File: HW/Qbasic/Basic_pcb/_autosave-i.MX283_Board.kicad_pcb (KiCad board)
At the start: 4 copper layers, 73 x 73 mm, 151 parts, among them P1 CONN_02X02, U11 ZLDO1117G33TA, X401 12MHz

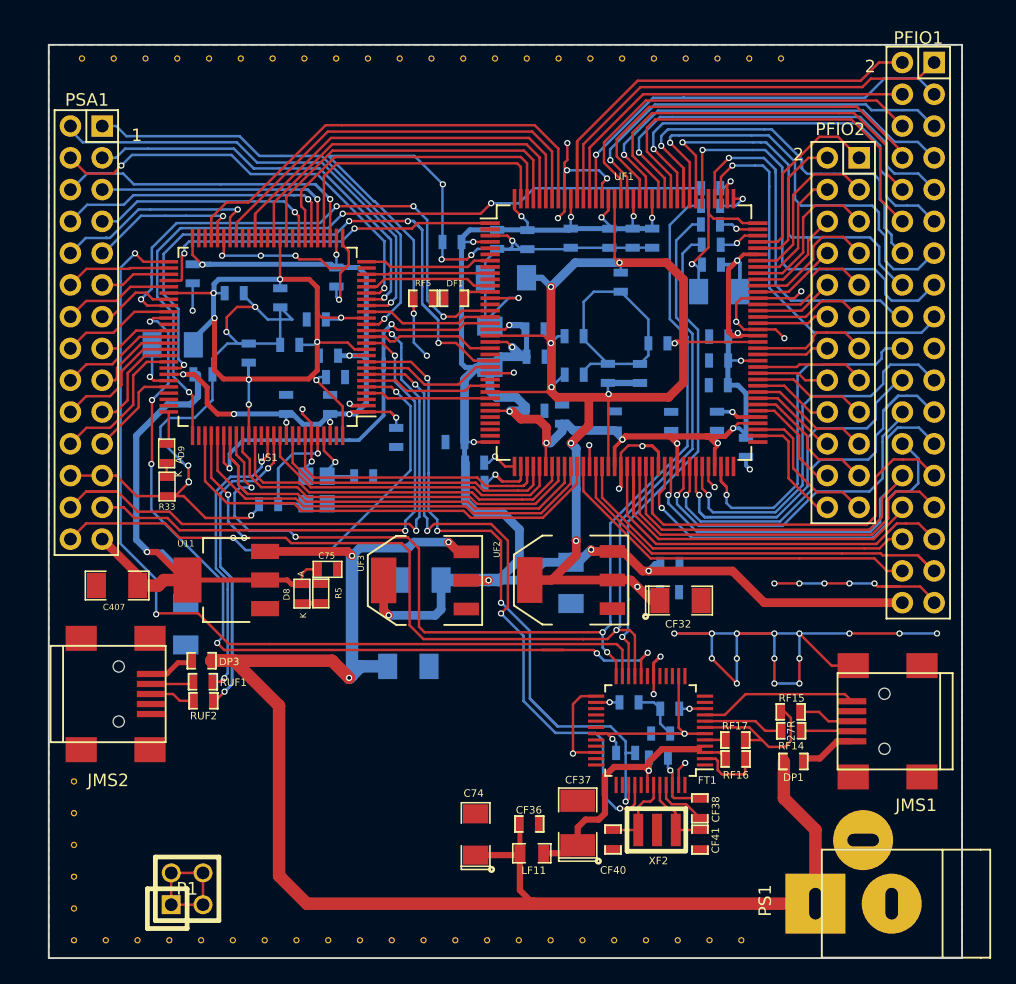
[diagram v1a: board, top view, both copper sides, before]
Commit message: last changes
all components placed, routes traced, ground shields missing
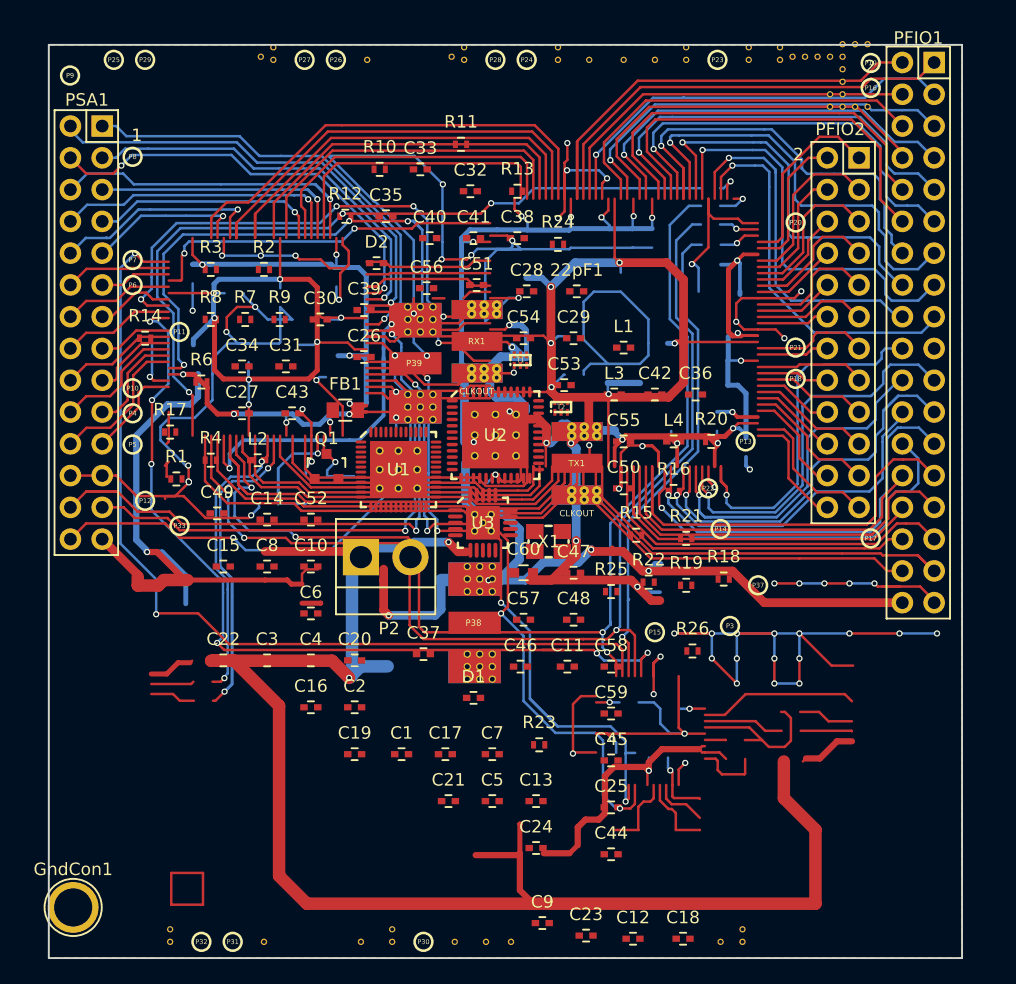
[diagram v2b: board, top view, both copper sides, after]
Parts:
- removed C396, C397, C398, C399, C400, C401, C404, C405, C408, C409, C410, CF1, CF10, CF11, CF12, CF13, CF16, CF17, CF18, CF19, CF2, CF20, CF23, CF24, CF25, CF26, CF27, CF3, CF4, CF5, CF6, CF7, CF8, CF9: 0.1uF, SM0603
- removed C402, C403: 20pF, SM0603
- removed C406, C411, CF14, CF21, CF28: 1uF, SM0603
- removed C407, C412: 4.7uF, SM1206
- removed C74, C76: 33uF, SM1206
- removed C75, CF31, CF33: 100n, SM0603
- removed CF15, CF22, CF29: 4.7uF, SM1206_Opendous
- removed CF30, CF32, CF34, CF35: 33uF, SM1206_Opendous
- removed CF36: 10nF, opendous:SM0603_Opendous
- removed CF37: 10uF, opendous:SM1210_Opendous
- removed CF38: 100nF, opendous:SM0603_Opendous
- removed CF39: 33nF, opendous:SM0603_Opendous
- removed CF40, CF41: 47pF, opendous:SM0603_Opendous
- removed D8, D9, DF1: LED, SM0603
- removed DP1, DP3: DIODE, opendous:SM0603_Opendous
- removed FT1: FT2232D, Housings_QFP:LQFP-48_7x7mm_Pitch0.5mm
- removed JMS1, JMS2: USB-MINI, Connect:USB_Mini-B
- removed LF11: HZ0805D152R-10, opendous:SM0805
- removed P1: CONN_02X02, hackrf:GSG-HEADER-2x2
- removed PS1: BARREL_JACK, Connect:JACK_ALIM
- removed R33, R5, RF5: 1k, SM0603
- removed RF1: 47k, SM0603
- removed RF14, RF15: 27R, opendous:SM0603_Opendous
- removed RF16: 10K, opendous:SM0603_Opendous
- removed RF17: 1K5, opendous:SM0603_Opendous
- removed RF18: 470R, opendous:SM0603_Opendous
- removed RF19, RF20: 10k, opendous:SM0603_Opendous
- removed RF2: 4.7k, SM0603
- removed RF21: 15K, opendous:SM0603_Opendous
- removed RF3, RF4, RF6, RF7: 68, SM0603
- removed RUF1, RUF2: 27, SM0603
- removed TH31, TH32, TH36, TH37: CONN_1, opendous:1Pin_12mil_VIA
- removed U11: ZLDO1117G33TA, LT1117
- removed UF1: XC6SLX9-2TQG144C, Housings_QFP:LQFP-144_20x20mm_Pitch0.5mm
- removed UF2: ZLDO1117G12TA, SMD_Packages:SOT-223
- removed UF3: ZLDO1117G33TA, SMD_Packages:SOT-223
- removed US1: ATSAM3S2CA-AU, Housings_QFP:LQFP-100_14x14mm_Pitch0.5mm
- removed X401: 12MHz, ABM8G
- removed XF2: 6MHz, resonator:CSTCR6M00G53Z
- added 22pF1: C_Small, Capacitors_SMD:C_0402, F.Cu at (61.5, 86.0)
- added C1: 22pF, Capacitors_SMD:C_0402, F.Cu at (47.5, 123.0)
- added C10: 22pF, Capacitors_SMD:C_0402, F.Cu at (40.2, 108.0)
- added C11: 10nF, Capacitors_SMD:C_0402, F.Cu at (60.8, 116.0)
- added C12: 100nF, Capacitors_SMD:C_0402, F.Cu at (66.0, 137.8)
- added C13: 2.2uF, Capacitors_SMD:C_0402, F.Cu at (58.2, 126.8)
- added C14: 100nF, Capacitors_SMD:C_0402, F.Cu at (36.8, 104.2)
- added C15: 2.2uF, Capacitors_SMD:C_0402, F.Cu at (33.2, 108.0)
- added C16: 100nF, Capacitors_SMD:C_0402, F.Cu at (40.2, 119.2)
- added C17: 2.2uF, Capacitors_SMD:C_0402, F.Cu at (51.0, 123.0)
- added C18: 100nF, Capacitors_SMD:C_0402, F.Cu at (70.0, 137.8)
- added C19: 2.2uF, Capacitors_SMD:C_0402, F.Cu at (43.8, 123.0)
- added C2: 22pF, Capacitors_SMD:C_0402, F.Cu at (43.8, 119.2)
- added C20: 100nF, Capacitors_SMD:C_0402, F.Cu at (43.8, 115.5)
- added C21: 2.2uF, Capacitors_SMD:C_0402, F.Cu at (51.2, 126.8)
- added C22: 100nF, Capacitors_SMD:C_0402, F.Cu at (33.2, 115.5)
- added C23: 2.2uF, Capacitors_SMD:C_0402, F.Cu at (62.2, 137.5)
- added C24: 100nF, Capacitors_SMD:C_0402, F.Cu at (58.2, 130.5)
- added C25: 100nF, Capacitors_SMD:C_0402, F.Cu at (64.2, 127.2)
- added C26: 22pF, Capacitors_SMD:C_0402, F.Cu at (44.5, 91.2)
- added C27: 22pF, Capacitors_SMD:C_0402, F.Cu at (34.8, 95.8)
- added C28: 330nF, Capacitors_SMD:C_0402, F.Cu at (57.5, 86.0)
- added C29: 330nF, Capacitors_SMD:C_0402, F.Cu at (61.2, 89.8)
- added C3: 22pF, Capacitors_SMD:C_0402, F.Cu at (36.8, 115.5)
- added C30: 10uF, Capacitors_SMD:C_0402, F.Cu at (41.0, 88.2)
- added C31: 22pF, Capacitors_SMD:C_0402, F.Cu at (38.2, 92.0)
- added C32: 330nF, Capacitors_SMD:C_0402, F.Cu at (53.0, 78.0)
- added C33: 22pF, Capacitors_SMD:C_0402, F.Cu at (49.0, 76.2)
- added C34: 22pF, Capacitors_SMD:C_0402, F.Cu at (34.8, 92.0)
- added C35: 22pF, Capacitors_SMD:C_0402, F.Cu at (46.2, 80.0)
- added C36: 3pF, Capacitors_SMD:C_0402, F.Cu at (71.0, 94.2)
- added C37: 1uF, Capacitors_SMD:C_0402, F.Cu at (49.2, 115.0)
- added C38: 22pF, Capacitors_SMD:C_0402, F.Cu at (56.8, 81.8)
- added C39: 22pF, Capacitors_SMD:C_0402, F.Cu at (44.5, 87.5)
- added C4: 10nF, Capacitors_SMD:C_0402, F.Cu at (40.2, 115.5)
- added C40: 22pF, Capacitors_SMD:C_0402, F.Cu at (49.8, 81.8)
- added C41: 22pF, Capacitors_SMD:C_0402, F.Cu at (53.2, 81.8)
- added C42: 3pF, Capacitors_SMD:C_0402, F.Cu at (67.8, 94.2)
- added C43: 180pF, Capacitors_SMD:C_0402, F.Cu at (38.8, 95.8)
- added C44: 100nF, Capacitors_SMD:C_0402, F.Cu at (64.2, 131.0)
- added C45: 100nF, Capacitors_SMD:C_0402, F.Cu at (64.2, 123.5)
- added C46: 2.2uF, Capacitors_SMD:C_0402, F.Cu at (57.0, 116.0)
- added C47: DNP, Capacitors_SMD:C_0402, F.Cu at (61.2, 108.5)
- added C48: DNP, Capacitors_SMD:C_0402, F.Cu at (61.2, 112.2)
- added C49: 33pF, Capacitors_SMD:C_0402, F.Cu at (32.8, 103.8)
- added C5: 10nF, Capacitors_SMD:C_0402, F.Cu at (54.8, 126.8)
- added C50: 3.3nF, Capacitors_SMD:C_0402, F.Cu at (65.2, 101.8)
- added C51: 100pF, Capacitors_SMD:C_0402, F.Cu at (53.5, 85.5)
- added C52: 47pF, Capacitors_SMD:C_0402, F.Cu at (40.2, 104.2)
- added C53: 100pF, Capacitors_SMD:C_0402, F.Cu at (60.5, 93.5)
- added C54: 100pF, Capacitors_SMD:C_0402, F.Cu at (57.2, 89.8)
- added C55: 100pF, Capacitors_SMD:C_0402, F.Cu at (65.2, 98.0)
- added C56: 100pF, Capacitors_SMD:C_0402, F.Cu at (49.5, 85.8)
- added C57: 100nF, Capacitors_SMD:C_0402, F.Cu at (57.2, 112.2)
- added C58: 100nF, Capacitors_SMD:C_0402, F.Cu at (64.2, 116.0)
- added C59: 100nF, Capacitors_SMD:C_0402, F.Cu at (64.2, 119.8)
- added C6: 100pF, Capacitors_SMD:C_0402, F.Cu at (40.2, 111.8)
- added C60: 100nF, Capacitors_SMD:C_0603, F.Cu at (57.2, 108.5)
- added C7: 100nF, Capacitors_SMD:C_0402, F.Cu at (54.8, 123.0)
- added C8: 10nF, Capacitors_SMD:C_0402, F.Cu at (36.8, 108.0)
- added C9: 10nF, Capacitors_SMD:C_0402, F.Cu at (58.8, 136.5)
- added D1: GSG-DIODE-TVS-BI, Capacitors_SMD:C_0402, F.Cu at (53.2, 118.5)
- added D2: GSG-DIODE-TVS-BI, Capacitors_SMD:C_0402, F.Cu at (45.5, 83.8)
- added FB1: FILTER, Capacitors_SMD:C_0805, F.Cu at (43.0, 95.5)
- added GndCon1: GND, Connect:1pin, F.Cu at (21.2, 135.2)
- added L1: DNP, Capacitors_SMD:C_0402, F.Cu at (65.2, 90.5)
- added L2: 6.2nH, Capacitors_SMD:C_0402, F.Cu at (36.0, 99.5)
- added L3: DNP, Capacitors_SMD:C_0402, F.Cu at (64.5, 94.2)
- added L4: DNP, Capacitors_SMD:C_0402, F.Cu at (69.2, 98.0)
- added P10: TXENABLE, hackrf1:GSG-TESTPOINT-50MIL-MASKONLY, F.Cu at (26.0, 93.8)
- added P11: RXENABLE, hackrf1:GSG-TESTPOINT-50MIL-MASKONLY, F.Cu at (29.8, 89.2)
- added P12: XTAL2, hackrf1:GSG-TESTPOINT-50MIL-MASKONLY, F.Cu at (27.0, 102.8)
- added P13: GCK1, hackrf1:GSG-TESTPOINT-50MIL-MASKONLY, F.Cu at (75.0, 98.0)
- added P14: GCK2, hackrf1:GSG-TESTPOINT-50MIL-MASKONLY, F.Cu at (73.0, 105.0)
- added P15: SGPIO_CLK, hackrf1:GSG-TESTPOINT-50MIL-MASKONLY, F.Cu at (67.8, 113.2)
- added P16: DA0, hackrf1:GSG-TESTPOINT-50MIL-MASKONLY, F.Cu at (85.0, 69.8)
- added P17: DA4, hackrf1:GSG-TESTPOINT-50MIL-MASKONLY, F.Cu at (85.0, 105.8)
- added P18: DA7, hackrf1:GSG-TESTPOINT-50MIL-MASKONLY, F.Cu at (79.0, 93.0)
- added P19: DD0, hackrf1:GSG-TESTPOINT-50MIL-MASKONLY, F.Cu at (85.0, 67.8)
- added P2: VAA, Pin_Headers:Pin_Header_Straight_1x02_Pitch3.96mm_Friction_Lock, F.Cu at (44.2, 107.2)
- added P20: DD5, hackrf1:GSG-TESTPOINT-50MIL-MASKONLY, F.Cu at (79.0, 80.5)
- added P21: DD9, hackrf1:GSG-TESTPOINT-50MIL-MASKONLY, F.Cu at (79.0, 90.5)
- added P22: RSSI, hackrf1:GSG-TESTPOINT-50MIL-MASKONLY, F.Cu at (72.0, 101.8)
- added P23: GND, hackrf1:GSG-TESTPOINT-50MIL-MASKONLY, F.Cu at (72.8, 67.5)
- added P24: GND, hackrf1:GSG-TESTPOINT-50MIL-MASKONLY, F.Cu at (57.5, 67.5)
- added P25: GND, hackrf1:GSG-TESTPOINT-50MIL-MASKONLY, F.Cu at (24.5, 67.5)
- added P26: GND, hackrf1:GSG-TESTPOINT-50MIL-MASKONLY, F.Cu at (42.2, 67.5)
- added P27: GND, hackrf1:GSG-TESTPOINT-50MIL-MASKONLY, F.Cu at (39.8, 67.5)
- added P28: GND, hackrf1:GSG-TESTPOINT-50MIL-MASKONLY, F.Cu at (55.0, 67.5)
- added P29: GND, hackrf1:GSG-TESTPOINT-50MIL-MASKONLY, F.Cu at (27.0, 67.5)
- added P3: SCL, hackrf1:GSG-TESTPOINT-50MIL-MASKONLY, F.Cu at (73.8, 112.8)
- added P30: GND, hackrf1:GSG-TESTPOINT-50MIL-MASKONLY, F.Cu at (49.2, 138.0)
- added P31: GND, hackrf1:GSG-TESTPOINT-50MIL-MASKONLY, F.Cu at (34.0, 138.0)
- added P32: GND, hackrf1:GSG-TESTPOINT-50MIL-MASKONLY, F.Cu at (31.5, 138.0)
- added P33: XCVR_CLKOUT, hackrf1:GSG-TESTPOINT-50MIL-MASKONLY, F.Cu at (29.8, 104.8)
- added P37: INTR, hackrf1:GSG-TESTPOINT-50MIL-MASKONLY, F.Cu at (76.0, 109.5)
- added P38: CLKIN, hackrf1:GSG-SMA-73251-2120, F.Cu at (51.2, 112.5)
- added P39: CLKOUT, hackrf1:GSG-SMA-73251-2120, F.Cu at (46.5, 91.8)
- added P4: SDA, hackrf1:GSG-TESTPOINT-50MIL-MASKONLY, F.Cu at (26.0, 95.8)
- added P5: SSP1_SCK, hackrf1:GSG-TESTPOINT-50MIL-MASKONLY, F.Cu at (26.0, 98.2)
- added P6: SSP1_MOSI, hackrf1:GSG-TESTPOINT-50MIL-MASKONLY, F.Cu at (26.0, 85.5)
- added P7: SSP1_MISO, hackrf1:GSG-TESTPOINT-50MIL-MASKONLY, F.Cu at (26.0, 83.5)
- added P8: CS_XCVR, hackrf1:GSG-TESTPOINT-50MIL-MASKONLY, F.Cu at (26.0, 75.2)
- added P9: CS_AD, hackrf1:GSG-TESTPOINT-50MIL-MASKONLY, F.Cu at (21.0, 68.8)
- added Q1: MOSFET_P, kicad1:SOT-23mos, F.Cu at (41.5, 100.0)
- added R1: 10k, Resistors_SMD:R_0402, F.Cu at (29.5, 101.0)
- added R10: 0, Resistors_SMD:R_0402, F.Cu at (45.8, 76.2)
- added R11: 0, Resistors_SMD:R_0402, F.Cu at (52.2, 74.2)
- added R12: 0, Resistors_SMD:R_0402, F.Cu at (43.0, 80.0)
- added R13: 0, Resistors_SMD:R_0402, F.Cu at (56.8, 78.0)
- added R14: 10k, Resistors_SMD:R_0402, F.Cu at (27.0, 89.8)
- added R15: 475, Resistors_SMD:R_0402, F.Cu at (66.2, 105.5)
- added R16: 475, Resistors_SMD:R_0402, F.Cu at (69.2, 102.0)
- added R17: 1k8, Resistors_SMD:R_0402, F.Cu at (29.0, 97.2)
- added R18: 1k8, Resistors_SMD:R_0402, F.Cu at (73.2, 109.0)
- added R19: 10k, Resistors_SMD:R_0402, F.Cu at (70.2, 109.5)
- added R2: 1k, Resistors_SMD:R_0402, F.Cu at (36.5, 84.2)
- added R20: 39, Resistors_SMD:R_0402, F.Cu at (72.2, 98.0)
- added R21: 39, Resistors_SMD:R_0402, F.Cu at (70.2, 105.8)
- added R22: 39, Resistors_SMD:R_0402, F.Cu at (67.2, 109.2)
- added R23: 10k, Resistors_SMD:R_0402, F.Cu at (58.5, 122.2)
- added R24: 39, Resistors_SMD:R_0402, F.Cu at (60.0, 82.2)
- added R25: 10k, Resistors_SMD:R_0402, F.Cu at (64.2, 110.0)
- added R26: 0, Resistors_SMD:R_0402, F.Cu at (70.8, 114.8)
- added R3: 1k, Resistors_SMD:R_0402, F.Cu at (32.2, 84.2)
- added R4: 1k, Resistors_SMD:R_0402, F.Cu at (32.2, 99.5)
- added R6: 4k7, Resistors_SMD:R_0402, F.Cu at (31.5, 93.2)
- added R7: 4k7, Resistors_SMD:R_0402, F.Cu at (35.0, 88.2)
- added R8: 4k7, Resistors_SMD:R_0402, F.Cu at (32.2, 88.2)
- added R9: 4k7, Resistors_SMD:R_0402, F.Cu at (37.8, 88.2)
- added RX1: CLKOUT, hackrf1:GSG-SMA-EDGE, F.Cu at (51.5, 90.0)
- added T1: RX_BALUN, hackrf1:GSG-2500BL14M100, F.Cu at (57.0, 91.5)
- added T2: TX_BALUN, hackrf1:GSG-2500BL14M100, F.Cu at (60.2, 95.2)
- added TX1: CLKOUT, hackrf1:GSG-SMA-EDGE, F.Cu at (59.5, 99.8)
- added U1: MAX2837, hackrf1:GSG-QFN48-6, F.Cu at (47.2, 100.2)
- added U2: MAX5864, hackrf1:GSG-QFN48-7, F.Cu at (55.0, 97.5)
- added U3: SI5351C, hackrf1:GSG-QFN20-4, F.Cu at (54.0, 104.5)
- added X1: GSG-XTAL4PIN, hackrf1:GSG-XTAL3.2x2.5mm, F.Cu at (59.2, 106.0)
- PFIO2: value CONN_02X13 -> CONN_02X12
- moved TH35 93.1 mm to (83.8, 66.2)
- moved TH12 88.0 mm to (75.2, 66.5)
- moved TH7 83.7 mm to (77.8, 66.5)
- moved TH10 76.9 mm to (62.5, 67.5)
- moved TH8 76.4 mm to (37.2, 66.5)
- moved TH20 75.9 mm to (77.8, 67.5)
- moved TH4 75.2 mm to (82.8, 67.2)
- moved TH5 75.2 mm to (36.2, 67.2)
- moved TH2 75.2 mm to (70.2, 66.5)
- moved TH6 74.1 mm to (51.5, 67.2)
- moved TH24 74.0 mm to (51.8, 138.0)
- moved TH16 73.2 mm to (78.8, 67.2)
- moved TH9 71.9 mm to (80.8, 67.2)
- moved TH43 71.8 mm to (73.0, 138.0)
- moved TH11 71.4 mm to (79.8, 67.2)
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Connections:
- PFIO1 pad 1: /spartan6/IO72 -> DA0
- PFIO1 pad 10: /spartan6/IO65 -> DD4
- PFIO1 pad 11: /spartan6/IO62 -> Net-(PFIO1-Pad11)
- PFIO1 pad 12: /spartan6/IO63 -> DD5
- PFIO1 pad 13: /spartan6/IO60 -> Net-(PFIO1-Pad13)
- PFIO1 pad 14: /spartan6/IO61 -> DD6
- PFIO1 pad 15: /spartan6/IO58 -> Net-(PFIO1-Pad15)
- PFIO1 pad 16: /spartan6/IO59 -> DD7
- PFIO1 pad 17: /spartan6/IO56 -> Net-(PFIO1-Pad17)
- PFIO1 pad 18: /spartan6/IO57 -> DD8
- PFIO1 pad 19: GND -> Net-(PFIO1-Pad19)
- PFIO1 pad 2: /spartan6/IO73 -> DD0
- PFIO1 pad 20: /spartan6/IO31 -> DD9
- PFIO1 pad 21: /spartan6/IO30 -> Net-(PFIO1-Pad21)
- PFIO1 pad 22: /spartan6/IO29 -> DA7
- PFIO1 pad 23: /spartan6/IO28 -> Net-(PFIO1-Pad23)
- PFIO1 pad 24: /spartan6/IO27 -> DA6
- PFIO1 pad 25: /spartan6/IO26 -> Net-(PFIO1-Pad25)
- PFIO1 pad 26: /spartan6/IO25 -> DA5
- PFIO1 pad 27: /spartan6/IO24 -> Net-(PFIO1-Pad27)
- PFIO1 pad 28: /spartan6/IO23 -> DA4
- PFIO1 pad 29: /spartan6/IO22 -> Net-(PFIO1-Pad29)
- PFIO1 pad 3: /spartan6/IO70 -> Net-(PFIO1-Pad3)
- PFIO1 pad 30: /spartan6/IO21 -> DA3
- PFIO1 pad 31: /spartan6/IO20 -> Net-(PFIO1-Pad31)
- PFIO1 pad 32: /spartan6/IO19 -> DA2
- PFIO1 pad 33: /spartan6/IO18 -> Net-(PFIO1-Pad33)
- PFIO1 pad 34: /spartan6/IO17 -> DA1
- PFIO1 pad 35: GND -> Net-(PFIO1-Pad35)
- PFIO1 pad 36: +3.3VDAC -> VCC
- PFIO1 pad 4: /spartan6/IO71 -> DD1
- PFIO1 pad 5: /spartan6/IO68 -> Net-(PFIO1-Pad5)
- PFIO1 pad 6: /spartan6/IO69 -> DD2
- PFIO1 pad 7: /spartan6/IO66 -> Net-(PFIO1-Pad7)
- PFIO1 pad 8: /spartan6/IO67 -> DD3
- PFIO1 pad 9: /spartan6/IO64 -> Net-(PFIO1-Pad9)
- PFIO2 pad 1: /spartan6/IO55 -> Net-(PFIO2-Pad1)
- PFIO2 pad 10: /spartan6/IO46 -> Net-(PFIO2-Pad10)
- PFIO2 pad 11: /spartan6/IO45 -> Net-(PFIO2-Pad11)
- PFIO2 pad 12: /spartan6/IO44 -> Net-(PFIO2-Pad12)
- PFIO2 pad 13: /spartan6/IO43 -> Net-(PFIO2-Pad13)
- PFIO2 pad 14: /spartan6/IO42 -> Net-(PFIO2-Pad14)
- PFIO2 pad 15: /spartan6/IO41 -> Net-(PFIO2-Pad15)
- PFIO2 pad 16: /spartan6/IO40 -> Net-(PFIO2-Pad16)
- PFIO2 pad 17: /spartan6/IO39 -> Net-(PFIO2-Pad17)
- PFIO2 pad 18: /spartan6/IO38 -> Net-(PFIO2-Pad18)
- PFIO2 pad 19: /spartan6/IO37 -> Net-(PFIO2-Pad19)
- PFIO2 pad 2: /spartan6/IO54 -> Net-(PFIO2-Pad2)
- PFIO2 pad 20: /spartan6/IO36 -> Net-(PFIO2-Pad20)
- PFIO2 pad 21: /spartan6/IO35 -> Net-(PFIO2-Pad21)
- PFIO2 pad 22: /spartan6/IO34 -> Net-(PFIO2-Pad22)
- PFIO2 pad 23: /spartan6/IO33 -> Net-(PFIO2-Pad23)
- PFIO2 pad 24: /spartan6/IO32 -> Net-(PFIO2-Pad24)
- PFIO2 pad 3: /spartan6/IO53 -> Net-(PFIO2-Pad3)
- PFIO2 pad 4: /spartan6/IO52 -> Net-(PFIO2-Pad4)
- PFIO2 pad 5: /spartan6/IO51 -> Net-(PFIO2-Pad5)
- PFIO2 pad 6: /spartan6/IO50 -> Net-(PFIO2-Pad6)
- PFIO2 pad 7: /spartan6/IO49 -> Net-(PFIO2-Pad7)
- PFIO2 pad 8: /spartan6/IO48 -> Net-(PFIO2-Pad8)
- PFIO2 pad 9: /spartan6/IO47 -> Net-(PFIO2-Pad9)
- PSA1 pad 1: /SAM3M/AD8 -> !VAA_ENABLE
- PSA1 pad 10: /SAM3M/UTXD0 -> Net-(PSA1-Pad10)
- PSA1 pad 11: /SAM3M/RXD0 -> SSP1_MISO
- PSA1 pad 12: /SAM3M/TXD0 -> SSP1_MOSI
- PSA1 pad 13: /SAM3M/PA27 -> Net-(PSA1-Pad13)
- PSA1 pad 14: /SAM3M/PA4 -> SCL
- PSA1 pad 15: /SAM3M/PC9 -> Net-(PSA1-Pad15)
- PSA1 pad 16: /SAM3M/PA28 -> XCVR_EN
- PSA1 pad 17: /SAM3M/PA30 -> Net-(PSA1-Pad17)
- PSA1 pad 18: /SAM3M/PA29 -> RXENABLE
- PSA1 pad 19: /SAM3M/PA3 -> SDA
- PSA1 pad 2: /SAM3M/AD2 -> CS_AD
- PSA1 pad 20: /SAM3M/PC10 -> TXENABLE
- PSA1 pad 21: /SAM3M/PC14 -> OEB
- PSA1 pad 22: /SAM3M/PA2 -> SSP1_SCK
- PSA1 pad 23: GND -> Net-(PSA1-Pad23)
- PSA1 pad 24: GND -> Net-(PSA1-Pad24)
- PSA1 pad 25: /SAM3M/AD0 -> Net-(PSA1-Pad25)
- PSA1 pad 26: /SAM3M/AD1 -> Net-(PSA1-Pad26)
- PSA1 pad 27: +3.3VP -> Net-(PSA1-Pad27)
- PSA1 pad 28: /SAM3M/AD5 -> Net-(PSA1-Pad28)
- PSA1 pad 3: /SAM3M/AD11 -> Net-(PSA1-Pad3)
- PSA1 pad 4: /SAM3M/AD9 -> CS_XCVR
- PSA1 pad 5: /SAM3M/PWML3 -> Net-(PSA1-Pad5)
- PSA1 pad 6: /SAM3M/PWML2 -> Net-(PSA1-Pad6)
- PSA1 pad 7: /SAM3M/PWMH2 -> Net-(PSA1-Pad7)
- PSA1 pad 8: /SAM3M/PWMH3 -> Net-(PSA1-Pad8)
- PSA1 pad 9: /SAM3M/URXD0 -> Net-(PSA1-Pad9)
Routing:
- net (no net): track 0.00 -> 892.5 mm, vias 0 -> 63
- net GND: track 347.6 -> 941.4 mm, vias 61 -> 56
- net Net-(C30-Pad1): track 0.00 -> 227.3 mm, vias 0 -> 14
- net +3.3VDAC: track 222.4 -> 0.00 mm, vias 22 -> 0
- net VAA: track 0.00 -> 176.0 mm, vias 0 -> 4
- net VDD5V: track 129.1 -> 0.00 mm, vias 3 -> 0
- net +3.3VP: track 121.2 -> 0.00 mm, vias 10 -> 0
- net +1V2: track 119.8 -> 0.00 mm, vias 9 -> 0
- net /spartan6/F_TCK: track 88.4 -> 0.00 mm, vias 4 -> 0
- net /spartan6/F_TMS: track 87.8 -> 0.00 mm, vias 3 -> 0
- net VCC: track 0.00 -> 80.0 mm
- net !VAA_ENABLE: track 0.00 -> 74.5 mm, vias 0 -> 1
- net /SAM3M/JTDI: track 74.3 -> 0.00 mm, vias 2 -> 0
- net /SAM3M/JNRST: track 70.4 -> 0.00 mm, vias 6 -> 0
- net +1.8V: track 67.4 -> 0.00 mm, vias 8 -> 0
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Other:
- board text removed: "A"
- board text removed: "K"

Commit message: version final antes de  planos de tierra
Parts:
- removed 22pF1: C_Small, Capacitors_SMD:C_0402
- removed C1, C10, C2, C26, C27, C3, C31, C33, C34, C35, C38, C39, C40, C41: 22pF, Capacitors_SMD:C_0402
- removed C11, C4, C5, C8, C9: 10nF, Capacitors_SMD:C_0402
- removed C12, C14, C16, C18, C20, C22, C24, C25, C44, C45, C57, C58, C59, C7: 100nF, Capacitors_SMD:C_0402
- removed C13, C15, C17, C19, C21, C23, C46: 2.2uF, Capacitors_SMD:C_0402
- removed C28, C29, C32: 330nF, Capacitors_SMD:C_0402
- removed C30: 10uF, Capacitors_SMD:C_0402
- removed C36, C42: 3pF, Capacitors_SMD:C_0402
- removed C37: 1uF, Capacitors_SMD:C_0402
- removed C43: 180pF, Capacitors_SMD:C_0402
- removed C47, C48, L1, L3, L4: DNP, Capacitors_SMD:C_0402
- removed C49: 33pF, Capacitors_SMD:C_0402
- removed C50: 3.3nF, Capacitors_SMD:C_0402
- removed C51, C53, C54, C55, C56, C6: 100pF, Capacitors_SMD:C_0402
- removed C52: 47pF, Capacitors_SMD:C_0402
- removed C60: 100nF, Capacitors_SMD:C_0603
- removed D1, D2: GSG-DIODE-TVS-BI, Capacitors_SMD:C_0402
- removed FB1: FILTER, Capacitors_SMD:C_0805
- removed GndCon1: GND, Connect:1pin
- removed L2: 6.2nH, Capacitors_SMD:C_0402
- removed P10: TXENABLE, hackrf1:GSG-TESTPOINT-50MIL-MASKONLY
- removed P11: RXENABLE, hackrf1:GSG-TESTPOINT-50MIL-MASKONLY
- removed P12: XTAL2, hackrf1:GSG-TESTPOINT-50MIL-MASKONLY
- removed P13: GCK1, hackrf1:GSG-TESTPOINT-50MIL-MASKONLY
- removed P14: GCK2, hackrf1:GSG-TESTPOINT-50MIL-MASKONLY
- removed P15: SGPIO_CLK, hackrf1:GSG-TESTPOINT-50MIL-MASKONLY
- removed P16: DA0, hackrf1:GSG-TESTPOINT-50MIL-MASKONLY
- removed P17: DA4, hackrf1:GSG-TESTPOINT-50MIL-MASKONLY
- removed P18: DA7, hackrf1:GSG-TESTPOINT-50MIL-MASKONLY
- removed P19: DD0, hackrf1:GSG-TESTPOINT-50MIL-MASKONLY
- removed P2: VAA, Pin_Headers:Pin_Header_Straight_1x02_Pitch3.96mm_Friction_Lock
- removed P20: DD5, hackrf1:GSG-TESTPOINT-50MIL-MASKONLY
- removed P21: DD9, hackrf1:GSG-TESTPOINT-50MIL-MASKONLY
- removed P22: RSSI, hackrf1:GSG-TESTPOINT-50MIL-MASKONLY
- removed P23, P24, P25, P26, P27, P28, P29, P30, P31, P32: GND, hackrf1:GSG-TESTPOINT-50MIL-MASKONLY
- removed P3: SCL, hackrf1:GSG-TESTPOINT-50MIL-MASKONLY
- removed P33: XCVR_CLKOUT, hackrf1:GSG-TESTPOINT-50MIL-MASKONLY
- removed P37: INTR, hackrf1:GSG-TESTPOINT-50MIL-MASKONLY
- removed P38: CLKIN, hackrf1:GSG-SMA-73251-2120
- removed P39: CLKOUT, hackrf1:GSG-SMA-73251-2120
- removed P4: SDA, hackrf1:GSG-TESTPOINT-50MIL-MASKONLY
- removed P5: SSP1_SCK, hackrf1:GSG-TESTPOINT-50MIL-MASKONLY
- removed P6: SSP1_MOSI, hackrf1:GSG-TESTPOINT-50MIL-MASKONLY
- removed P7: SSP1_MISO, hackrf1:GSG-TESTPOINT-50MIL-MASKONLY
- removed P8: CS_XCVR, hackrf1:GSG-TESTPOINT-50MIL-MASKONLY
- removed P9: CS_AD, hackrf1:GSG-TESTPOINT-50MIL-MASKONLY
- removed Q1: MOSFET_P, kicad1:SOT-23mos
- removed R1, R14, R19, R23, R25: 10k, Resistors_SMD:R_0402
- removed R10, R11, R12, R13, R26: 0, Resistors_SMD:R_0402
- removed R15, R16: 475, Resistors_SMD:R_0402
- removed R17, R18: 1k8, Resistors_SMD:R_0402
- removed R2, R3, R4: 1k, Resistors_SMD:R_0402
- removed R20, R21, R22, R24: 39, Resistors_SMD:R_0402
- removed R6, R7, R8, R9: 4k7, Resistors_SMD:R_0402
- removed RX1, TX1: CLKOUT, hackrf1:GSG-SMA-EDGE
- removed T1: RX_BALUN, hackrf1:GSG-2500BL14M100
- removed T2: TX_BALUN, hackrf1:GSG-2500BL14M100
- removed U1: MAX2837, hackrf1:GSG-QFN48-6
- removed U2: MAX5864, hackrf1:GSG-QFN48-7
- removed U3: SI5351C, hackrf1:GSG-QFN20-4
- removed X1: GSG-XTAL4PIN, hackrf1:GSG-XTAL3.2x2.5mm
- added C396: 0.1uF, SM0603, B.Cu at (34.1, 86.2)
- added C397: 0.1uF, SM0603, B.Cu at (38.6, 90.3)
- added C398: 0.1uF, SM0603, B.Cu at (41.8, 95.0)
- added C399: 0.1uF, SM0603, B.Cu at (41.7, 91.2)
- added C400: 0.1uF, SM0603, B.Cu at (38.3, 95.0)
- added C401: 0.1uF, SM0603, B.Cu at (42.3, 84.9)
- added C402: 20pF, SM0603, B.Cu at (44.5, 100.8)
- added C403: 20pF, SM0603, B.Cu at (36.9, 103.0)
- added C404: 0.1uF, SM0603, B.Cu at (30.8, 84.6)
- added C405: 0.1uF, SM0603, B.Cu at (31.6, 92.6)
- added C406: 1uF, SM0603, B.Cu at (47.1, 97.7)
- added C407: 4.7uF, SM1206, F.Cu at (24.8, 109.5)
- added C408: 0.1uF, SM0603, B.Cu at (35.3, 90.9)
- added C409: 0.1uF, SM0603, B.Cu at (42.2, 92.9)
- added C410: 0.1uF, SM0603, B.Cu at (40.7, 88.2)
- added C411: 1uF, SM0603, B.Cu at (37.8, 86.5)
- added C412: 4.7uF, SM1206, B.Cu at (29.2, 90.3)
- added C74: 33uF, SM1206, F.Cu at (53.4, 129.4)
- added C75: 100n, SM0603, F.Cu at (41.6, 108.2)
- added C76: 33uF, SM1206, B.Cu at (30.2, 112.6)
- added CF1: 0.1uF, SM0603, B.Cu at (75.0, 98.5)
- added CF10: 0.1uF, SM0603, B.Cu at (58.2, 91.2)
- added CF11: 0.1uF, SM0603, B.Cu at (51.5, 82.1)
- added CF12: 0.1uF, SM0603, B.Cu at (67.5, 81.8)
- added CF13: 0.1uF, SM0603, B.Cu at (55.1, 81.8)
- added CF14: 1uF, SM0603, B.Cu at (61.0, 81.8)
- added CF15: 4.7uF, SM1206_Opendous, B.Cu at (54.6, 90.4)
- added CF16: 0.1uF, SM0603, B.Cu at (58.2, 95.5)
- added CF17: 0.1uF, SM0603, B.Cu at (60.3, 95.8)
- added CF18: 0.1uF, SM0603, B.Cu at (69.0, 96.4)
- added CF19: 0.1uF, SM0603, B.Cu at (64.5, 96.4)
- added CF2: 0.1uF, SM0603, B.Cu at (51.8, 98.0)
- added CF20: 0.1uF, SM0603, B.Cu at (72.3, 83.9)
- added CF21: 1uF, SM0603, B.Cu at (72.8, 93.5)
- added CF22: 4.7uF, SM1206_Opendous, B.Cu at (61.0, 109.3)
- added CF23: 0.1uF, SM0603, B.Cu at (61.3, 89.6)
- added CF24: 0.1uF, SM0603, B.Cu at (61.3, 92.7)
- added CF25: 0.1uF, SM0603, B.Cu at (66.6, 92.6)
- added CF26: 0.1uF, SM0603, B.Cu at (68.9, 110.0)
- added CF27: 0.1uF, SM0603, B.Cu at (68.0, 90.2)
- added CF28: 1uF, SM0603, B.Cu at (64.0, 92.6)
- added CF29: 4.7uF, SM1206_Opendous, B.Cu at (55.8, 84.9)
- added CF3: 0.1uF, SM0603, B.Cu at (72.7, 96.4)
- added CF30: 33uF, SM1206_Opendous, B.Cu at (49.0, 109.1)
- added CF31: 100n, SM0603, B.Cu at (65.0, 85.3)
- added CF32: 33uF, SM1206_Opendous, F.Cu at (69.8, 110.7)
- added CF33: 100n, SM0603, B.Cu at (72.8, 89.6)
- added CF34: 33uF, SM1206_Opendous, B.Cu at (72.9, 86.0)
- added CF35: 33uF, SM1206_Opendous, B.Cu at (48.0, 116.0)
- added CF36: 10nF, opendous:SM0603_Opendous, F.Cu at (57.7, 128.6)
- added CF37: 10uF, opendous:SM1210_Opendous, F.Cu at (61.6, 128.5)
- added CF38: 100nF, opendous:SM0603_Opendous, F.Cu at (71.3, 127.3)
- added CF39: 33nF, opendous:SM0603_Opendous, B.Cu at (68.2, 121.3)
- added CF4: 0.1uF, SM0603, B.Cu at (57.6, 81.9)
- added CF40: 47pF, opendous:SM0603_Opendous, F.Cu at (64.4, 129.8)
- added CF41: 47pF, opendous:SM0603_Opendous, F.Cu at (71.3, 129.8)
- added CF5: 0.1uF, SM0603, B.Cu at (72.8, 91.5)
- added CF6: 0.1uF, SM0603, B.Cu at (64.1, 81.8)
- added CF7: 0.1uF, SM0603, B.Cu at (58.2, 89.0)
- added CF8: 0.1uF, SM0603, B.Cu at (69.0, 107.8)
- added CF9: 0.1uF, SM0603, B.Cu at (66.0, 81.8)
- added D8: LED, SM0603, F.Cu at (39.5, 110.2)
- added D9: LED, SM0603, F.Cu at (28.7, 99.0)
- added DF1: LED, SM0603, F.Cu at (51.7, 86.6)
- added DP1: DIODE, opendous:SM0603_Opendous, F.Cu at (78.8, 123.6)
- added DP3: DIODE, opendous:SM0603_Opendous, F.Cu at (31.5, 115.5)
- added FT1: FT2232D, Housings_QFP:LQFP-48_7x7mm_Pitch0.5mm, F.Cu at (67.4, 121.1)
- added JMS1: USB-MINI, Connect:USB_Mini-B, F.Cu at (87.0, 120.4)
- added JMS2: USB-MINI, Connect:USB_Mini-B, F.Cu at (24.0, 118.2)
- added LF11: HZ0805D152R-10, opendous:SM0805, F.Cu at (57.9, 130.9)
- added P1: CONN_02X02, hackrf:GSG-HEADER-2x2, F.Cu at (30.4, 133.8)
- added PS1: BARREL_JACK, Connect:JACK_ALIM, F.Cu at (86.7, 134.9)
- added R33: 1k, SM0603, F.Cu at (28.8, 101.6)
- added R5: 1k, SM0603, F.Cu at (41.0, 110.2)
- added RF1: 47k, SM0603, B.Cu at (53.3, 99.7)
- added RF14: 27R, opendous:SM0603_Opendous, F.Cu at (78.6, 121.1)
- added RF15: 27R, opendous:SM0603_Opendous, F.Cu at (78.6, 119.6)
- added RF16: 10K, opendous:SM0603_Opendous, F.Cu at (74.2, 123.4)
- added RF17: 1K5, opendous:SM0603_Opendous, F.Cu at (74.2, 121.9)
- added RF18: 470R, opendous:SM0603_Opendous, B.Cu at (68.0, 123.3)
- added RF19: 10k, opendous:SM0603_Opendous, B.Cu at (68.9, 119.4)
- added RF2: 4.7k, SM0603, B.Cu at (53.4, 101.3)
- added RF20: 10k, opendous:SM0603_Opendous, B.Cu at (65.7, 118.9)
- added RF21: 15K, opendous:SM0603_Opendous, B.Cu at (65.4, 122.9)
- added RF3: 68, SM0603, B.Cu at (72.2, 77.8)
- added RF4: 68, SM0603, B.Cu at (72.2, 79.2)
- added RF5: 1k, SM0603, F.Cu at (49.2, 86.6)
- added RF6: 68, SM0603, B.Cu at (72.2, 80.7)
- added RF7: 68, SM0603, B.Cu at (72.2, 82.3)
- added RUF1: 27, SM0603, F.Cu at (31.6, 117.2)
- added RUF2: 27, SM0603, F.Cu at (31.7, 118.7)
- added TH31: CONN_1, opendous:1Pin_12mil_VIA, F.Cu at (21.3, 125.2)
- added TH32: CONN_1, opendous:1Pin_12mil_VIA, F.Cu at (21.3, 130.3)
- added TH36: CONN_1, opendous:1Pin_12mil_VIA, F.Cu at (21.3, 132.8)
- added TH37: CONN_1, opendous:1Pin_12mil_VIA, F.Cu at (21.3, 127.7)
- added U11: ZLDO1117G33TA, LT1117, F.Cu at (33.5, 109.1)
- added UF1: XC6SLX9-2TQG144C, Housings_QFP:LQFP-144_20x20mm_Pitch0.5mm, F.Cu at (65.3, 89.3)
- added UF2: ZLDO1117G12TA, SMD_Packages:SOT-223, F.Cu at (61.0, 109.1)
- added UF3: ZLDO1117G33TA, SMD_Packages:SOT-223, F.Cu at (49.4, 109.1)
- added US1: ATSAM3S2CA-AU, Housings_QFP:LQFP-100_14x14mm_Pitch0.5mm, F.Cu at (36.8, 89.6)
- added X401: 12MHz, ABM8G, B.Cu at (41.5, 100.8)
- added XF2: 6MHz, resonator:CSTCR6M00G53Z, F.Cu at (67.9, 129.1)
- PFIO2: value CONN_02X12 -> CONN_02X13
- moved TH35 93.1 mm to (21.3, 135.3)
- moved TH12 88.0 mm to (23.9, 137.9)
- moved TH7 83.7 mm to (34.0, 137.9)
- moved TH10 76.9 mm to (31.5, 137.9)
- moved TH8 76.4 mm to (64.5, 137.9)
- moved TH20 75.9 mm to (49.3, 137.9)
- moved TH4 75.2 mm to (56.9, 137.9)
- moved TH5 75.2 mm to (62.0, 137.9)
- moved TH2 75.2 mm to (46.7, 137.9)
- moved TH6 74.1 mm to (28.9, 137.9)
- moved TH24 74.0 mm to (29.6, 67.4)
- moved TH16 73.2 mm to (59.4, 137.9)
- moved TH9 71.9 mm to (67.0, 137.9)
- moved TH43 71.8 mm to (60.0, 67.4)
- moved TH11 71.4 mm to (69.6, 137.9)
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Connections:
- PFIO1 pad 1: DA0 -> /spartan6/IO72
- PFIO1 pad 10: DD4 -> /spartan6/IO65
- PFIO1 pad 11: Net-(PFIO1-Pad11) -> /spartan6/IO62
- PFIO1 pad 12: DD5 -> /spartan6/IO63
- PFIO1 pad 13: Net-(PFIO1-Pad13) -> /spartan6/IO60
- PFIO1 pad 14: DD6 -> /spartan6/IO61
- PFIO1 pad 15: Net-(PFIO1-Pad15) -> /spartan6/IO58
- PFIO1 pad 16: DD7 -> /spartan6/IO59
- PFIO1 pad 17: Net-(PFIO1-Pad17) -> /spartan6/IO56
- PFIO1 pad 18: DD8 -> /spartan6/IO57
- PFIO1 pad 19: Net-(PFIO1-Pad19) -> GND
- PFIO1 pad 2: DD0 -> /spartan6/IO73
- PFIO1 pad 20: DD9 -> /spartan6/IO31
- PFIO1 pad 21: Net-(PFIO1-Pad21) -> /spartan6/IO30
- PFIO1 pad 22: DA7 -> /spartan6/IO29
- PFIO1 pad 23: Net-(PFIO1-Pad23) -> /spartan6/IO28
- PFIO1 pad 24: DA6 -> /spartan6/IO27
- PFIO1 pad 25: Net-(PFIO1-Pad25) -> /spartan6/IO26
- PFIO1 pad 26: DA5 -> /spartan6/IO25
- PFIO1 pad 27: Net-(PFIO1-Pad27) -> /spartan6/IO24
- PFIO1 pad 28: DA4 -> /spartan6/IO23
- PFIO1 pad 29: Net-(PFIO1-Pad29) -> /spartan6/IO22
- PFIO1 pad 3: Net-(PFIO1-Pad3) -> /spartan6/IO70
- PFIO1 pad 30: DA3 -> /spartan6/IO21
- PFIO1 pad 31: Net-(PFIO1-Pad31) -> /spartan6/IO20
- PFIO1 pad 32: DA2 -> /spartan6/IO19
- PFIO1 pad 33: Net-(PFIO1-Pad33) -> /spartan6/IO18
- PFIO1 pad 34: DA1 -> /spartan6/IO17
- PFIO1 pad 35: Net-(PFIO1-Pad35) -> GND
- PFIO1 pad 36: VCC -> +3.3VDAC
- PFIO1 pad 4: DD1 -> /spartan6/IO71
- PFIO1 pad 5: Net-(PFIO1-Pad5) -> /spartan6/IO68
- PFIO1 pad 6: DD2 -> /spartan6/IO69
- PFIO1 pad 7: Net-(PFIO1-Pad7) -> /spartan6/IO66
- PFIO1 pad 8: DD3 -> /spartan6/IO67
- PFIO1 pad 9: Net-(PFIO1-Pad9) -> /spartan6/IO64
- PFIO2 pad 1: Net-(PFIO2-Pad1) -> /spartan6/IO55
- PFIO2 pad 10: Net-(PFIO2-Pad10) -> /spartan6/IO46
- PFIO2 pad 11: Net-(PFIO2-Pad11) -> /spartan6/IO45
- PFIO2 pad 12: Net-(PFIO2-Pad12) -> /spartan6/IO44
- PFIO2 pad 13: Net-(PFIO2-Pad13) -> /spartan6/IO43
- PFIO2 pad 14: Net-(PFIO2-Pad14) -> /spartan6/IO42
- PFIO2 pad 15: Net-(PFIO2-Pad15) -> /spartan6/IO41
- PFIO2 pad 16: Net-(PFIO2-Pad16) -> /spartan6/IO40
- PFIO2 pad 17: Net-(PFIO2-Pad17) -> /spartan6/IO39
- PFIO2 pad 18: Net-(PFIO2-Pad18) -> /spartan6/IO38
- PFIO2 pad 19: Net-(PFIO2-Pad19) -> /spartan6/IO37
- PFIO2 pad 2: Net-(PFIO2-Pad2) -> /spartan6/IO54
- PFIO2 pad 20: Net-(PFIO2-Pad20) -> /spartan6/IO36
- PFIO2 pad 21: Net-(PFIO2-Pad21) -> /spartan6/IO35
- PFIO2 pad 22: Net-(PFIO2-Pad22) -> /spartan6/IO34
- PFIO2 pad 23: Net-(PFIO2-Pad23) -> /spartan6/IO33
- PFIO2 pad 24: Net-(PFIO2-Pad24) -> /spartan6/IO32
- PFIO2 pad 3: Net-(PFIO2-Pad3) -> /spartan6/IO53
- PFIO2 pad 4: Net-(PFIO2-Pad4) -> /spartan6/IO52
- PFIO2 pad 5: Net-(PFIO2-Pad5) -> /spartan6/IO51
- PFIO2 pad 6: Net-(PFIO2-Pad6) -> /spartan6/IO50
- PFIO2 pad 7: Net-(PFIO2-Pad7) -> /spartan6/IO49
- PFIO2 pad 8: Net-(PFIO2-Pad8) -> /spartan6/IO48
- PFIO2 pad 9: Net-(PFIO2-Pad9) -> /spartan6/IO47
- PSA1 pad 1: !VAA_ENABLE -> /SAM3M/AD8
- PSA1 pad 10: Net-(PSA1-Pad10) -> /SAM3M/UTXD0
- PSA1 pad 11: SSP1_MISO -> /SAM3M/RXD0
- PSA1 pad 12: SSP1_MOSI -> /SAM3M/TXD0
- PSA1 pad 13: Net-(PSA1-Pad13) -> /SAM3M/PA27
- PSA1 pad 14: SCL -> /SAM3M/PA4
- PSA1 pad 15: Net-(PSA1-Pad15) -> /SAM3M/PC9
- PSA1 pad 16: XCVR_EN -> /SAM3M/PA28
- PSA1 pad 17: Net-(PSA1-Pad17) -> /SAM3M/PA30
- PSA1 pad 18: RXENABLE -> /SAM3M/PA29
- PSA1 pad 19: SDA -> /SAM3M/PA3
- PSA1 pad 2: CS_AD -> /SAM3M/AD2
- PSA1 pad 20: TXENABLE -> /SAM3M/PC10
- PSA1 pad 21: OEB -> /SAM3M/PC14
- PSA1 pad 22: SSP1_SCK -> /SAM3M/PA2
- PSA1 pad 23: Net-(PSA1-Pad23) -> GND
- PSA1 pad 24: Net-(PSA1-Pad24) -> GND
- PSA1 pad 25: Net-(PSA1-Pad25) -> /SAM3M/AD0
- PSA1 pad 26: Net-(PSA1-Pad26) -> /SAM3M/AD1
- PSA1 pad 27: Net-(PSA1-Pad27) -> +3.3VP
- PSA1 pad 28: Net-(PSA1-Pad28) -> /SAM3M/AD5
- PSA1 pad 3: Net-(PSA1-Pad3) -> /SAM3M/AD11
- PSA1 pad 4: CS_XCVR -> /SAM3M/AD9
- PSA1 pad 5: Net-(PSA1-Pad5) -> /SAM3M/PWML3
- PSA1 pad 6: Net-(PSA1-Pad6) -> /SAM3M/PWML2
- PSA1 pad 7: Net-(PSA1-Pad7) -> /SAM3M/PWMH2
- PSA1 pad 8: Net-(PSA1-Pad8) -> /SAM3M/PWMH3
- PSA1 pad 9: Net-(PSA1-Pad9) -> /SAM3M/URXD0
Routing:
- net (no net): track 892.5 -> 0.00 mm, vias 63 -> 0
- net GND: track 941.4 -> 347.6 mm, vias 56 -> 61
- net Net-(C30-Pad1): track 227.3 -> 0.00 mm, vias 14 -> 0
- net +3.3VDAC: track 0.00 -> 222.4 mm, vias 0 -> 22
- net VAA: track 176.0 -> 0.00 mm, vias 4 -> 0
- net VDD5V: track 0.00 -> 129.1 mm, vias 0 -> 3
- net +3.3VP: track 0.00 -> 121.2 mm, vias 0 -> 10
- net +1V2: track 0.00 -> 119.8 mm, vias 0 -> 9
- net /spartan6/F_TCK: track 0.00 -> 88.4 mm, vias 0 -> 4
- net /spartan6/F_TMS: track 0.00 -> 87.8 mm, vias 0 -> 3
- net VCC: track 80.0 -> 0.00 mm
- net !VAA_ENABLE: track 74.5 -> 0.00 mm, vias 1 -> 0
- net /SAM3M/JTDI: track 0.00 -> 74.3 mm, vias 0 -> 2
- net /SAM3M/JNRST: track 0.00 -> 70.4 mm, vias 0 -> 6
- net +1.8V: track 0.00 -> 67.4 mm, vias 0 -> 8
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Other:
- board text added: "A"
- board text added: "K"
